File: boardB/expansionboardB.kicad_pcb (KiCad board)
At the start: 4 copper layers, 131 x 83.8 mm, 60 parts, among them J1 USB_C_Receptacle, J2 2086581051, SW1 ESPRST, SW4 ESPPROG, U1 ESP32-S3-WROOM-1, U2 GPIO_U2, U4 GPIO_U4, U5 SII1136CTU, U7 MAX20022ATIA+T, t1V2 1V2_TEST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

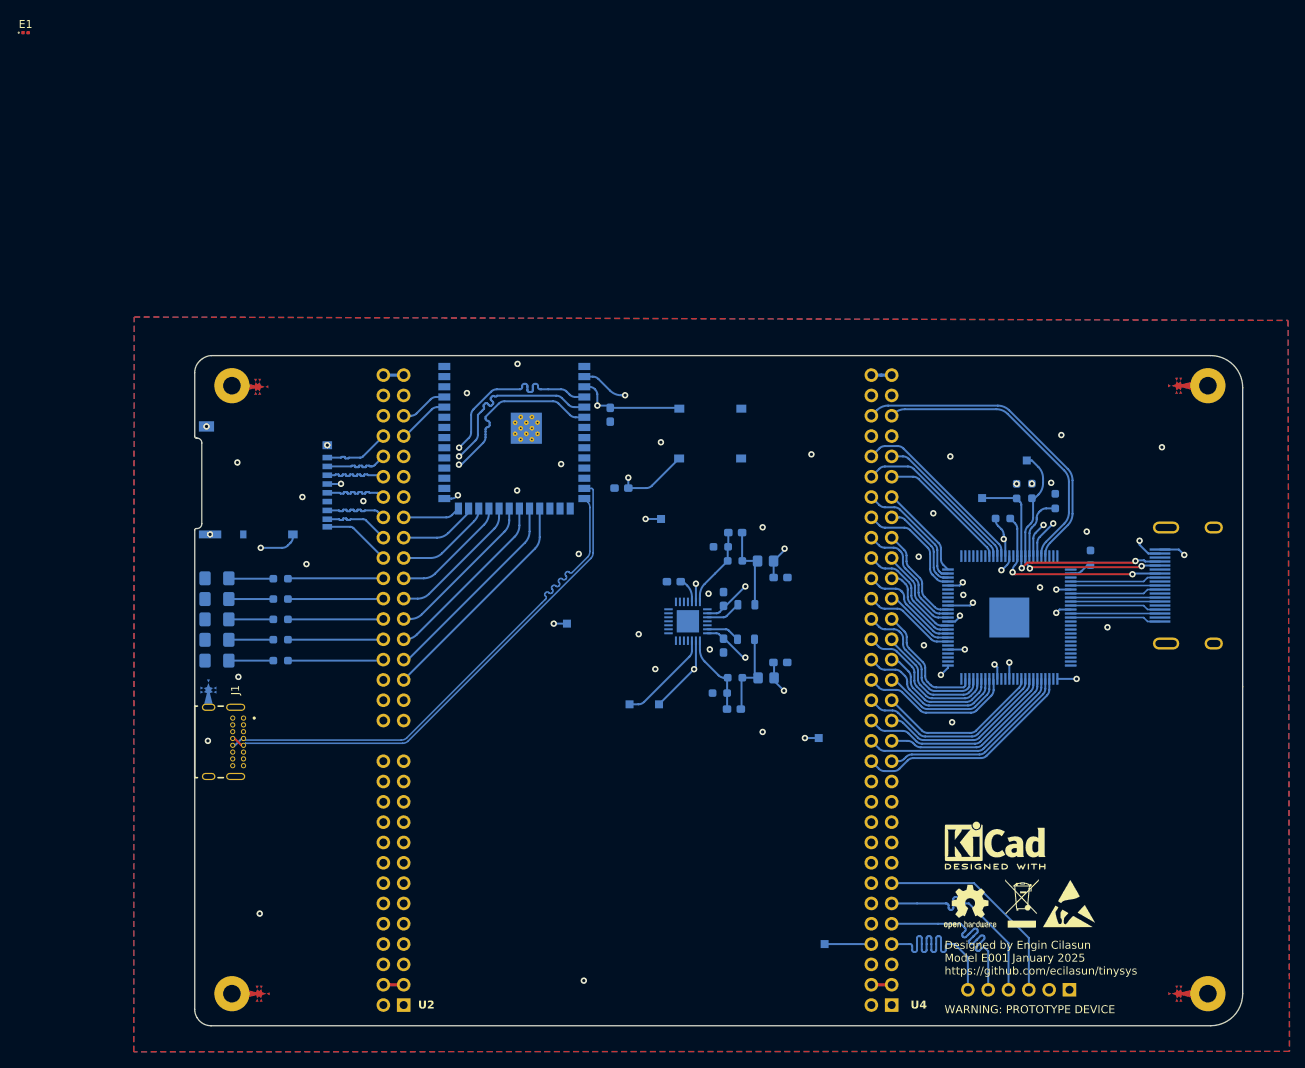
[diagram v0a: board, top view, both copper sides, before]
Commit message: Board B reshaped
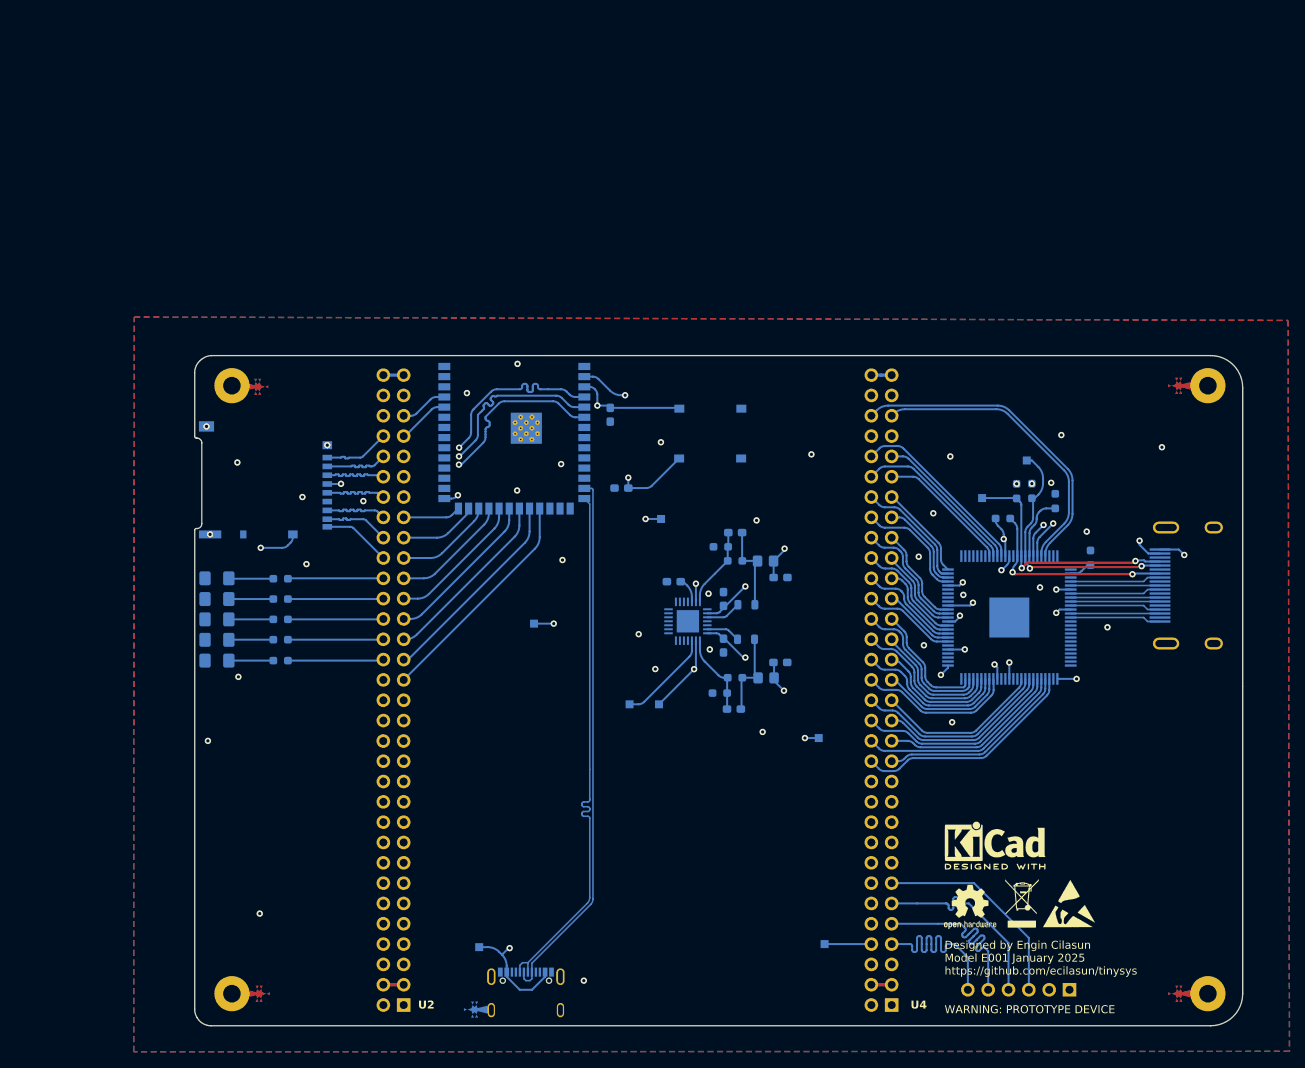
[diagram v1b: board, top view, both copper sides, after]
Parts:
- removed E1: SparkGap, Diode_SMD:D_0201_0603Metric
- removed J1: USB_C_Receptacle, USB4085-GF-A_REVA4:GCT_USB4085-GF-A_REVA4
- added J3: 12402012E212A, 12402012E212A:AMPHENOL_12402012E212A, B.Cu at (63.5, 122.6)
- added t5V2: 5V_IN_TEST, TestPoint:TestPoint_Pad_1.0x1.0mm, B.Cu at (57.7, 114.7)
- moved t5V1 4.11 mm to (64.5, 74.2), turned to 0 degrees
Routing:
- net 5V: track 22.4 -> 37.2 mm, vias 6 -> 7
- net ESP2D_P: track 64.4 -> 67.7 mm
- net ESP2D_N: track 64.6 -> 67.4 mm
